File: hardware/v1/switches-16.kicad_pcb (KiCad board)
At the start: 2 copper layers, 200.7 x 34.3 mm, 18 parts, among them P1 CONN_02X02, SW1 SWITCH_INV, SW10 SWITCH_INV, SW11 SWITCH_INV, SW12 SWITCH_INV, SW13 SWITCH_INV, SW14 SWITCH_INV, SW15 SWITCH_INV, SW16 SWITCH_INV, SW2 SWITCH_INV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

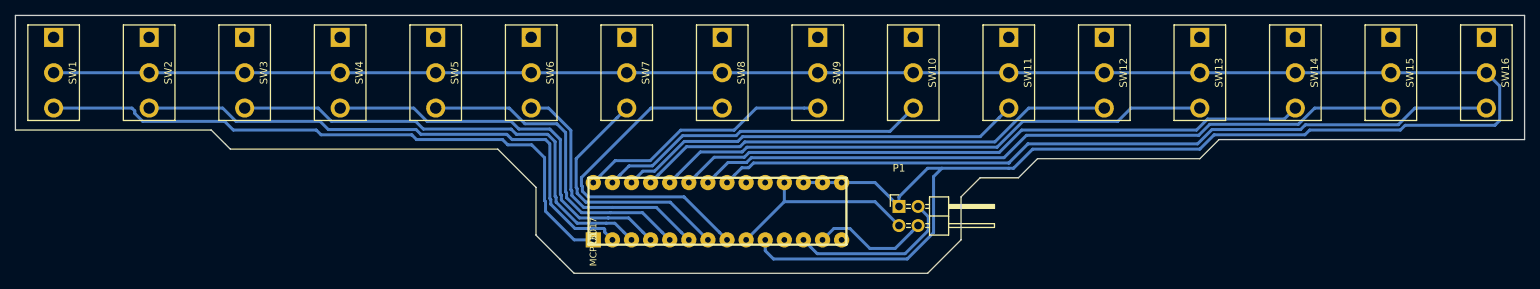
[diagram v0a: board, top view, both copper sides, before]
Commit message: fix missing connections in switches-16
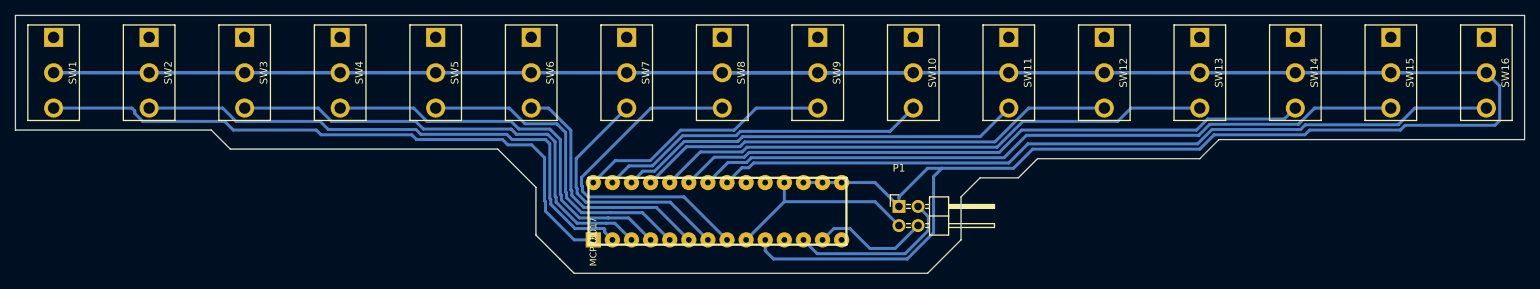
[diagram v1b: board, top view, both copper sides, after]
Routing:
- net GND: track 331.7 -> 540.0 mm

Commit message: replace switch footprints in switches-16
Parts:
- SW1, SW10, SW11, SW12, SW13, SW14, SW15, SW16, SW2, SW3, SW4, SW5, SW6, SW7, SW8, SW9: footprint myparts:SW_SPDT -> myparts:SW_SPDT-custom
